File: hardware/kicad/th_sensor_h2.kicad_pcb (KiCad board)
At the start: 2 copper layers, 72 x 58 mm, 74 parts, among them J1 DEBUG, Q1 AO3401A, Q2 AO3401A, Q3 2N7002, Q4 2N7002, SW1 USER/BOOT, SW2 RST, U1 TPS63900DSKR, U2 TPS63900DSKR, U3 TPS3839K33DBZR, U4 ESP32-H2-MINI-1-H4S, U5 SHT40-AD1B-R3, Y1 32.768kHz

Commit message: Finish PCB: silkscreen placement, fab outputs, check reports
- gen_pcb.py: reference designators placed clear of pads, other silk
  and courtyards (rasterised, so concave holder courtyards work); 21
  dense-area references stay on F.Fab only. Cell warning between the
  holders, J1 pinout on the back, tented vias, aux origin at the board
  corner, stitching vias kept clear of pads.
- gen_production.py: Gerber X2 + Excellon (zip), JLC BOM with a dated
  stock/library snapshot, JLC CPL, pad-1 orientation checklist for the
  placement preview, assembly drawing, manufacturing blockers (module
  stock is 0 at JLC on 2026-10-29).
- gen_reports.py: ERC, DRC with schematic parity (0 violations, 0
  unconnected, 0 footprint errors), schematic PDF, 2D/3D renders.

Co-Authored-By: Claude Opus 5.5 <noreply@anthropic.com>
Claude-Session: https://claude.ai/code/session_01TvrXHUQLozvfXGbtsTcbbw
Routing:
- net GND: vias 176 -> 169
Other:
- outline, holes or cut-outs redrawn
- board text added: "2 x CR2032 (one TPS63900 buck-boost per cell)"
- board text added: "3V3"
- board text added: "BOOT"
- board text added: "CR2032 ONLY"
- board text added: "D+"
- board text added: "D-"
- board text added: "ESP32-H2 Matter/Thread temperature & humidity"
- board text added: "GND"
- board text added: "J1 debug (not fitted): 3V3 pad powers the board only with JP1 closed"
- board text added: "NO RECHARGE"
- board text added: "Primary lithium cells only - never recharge"
- board text added: "RX"
- board text added: "TX"
- board text removed: "+"
- board text removed: "2 x CR2032 in parallel through one buck-boost each - do not recharge"
- board text removed: "CR2032 ONLY - NO CHARGE"
- board text removed: "TX RX D+ D- BOOT 3V3 GND"

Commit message: Add EN test pad and net-name test pad labels; reproducible PCB output
Hardware
- TP11 on EN next to the reset button (schematic + PCB); TP9 (GND) moved
  to make room. Schematic: split the EN wire at the new T so kicad-cli
  connects it; fix stale notes (GPIO12 enables the dividers, EN is on
  TP11, not on J1).
- Silkscreen: every test pad shows its net name (VBAT1, VBAT2, VIN1/2,
  VOUT1/2, 3V3_PWR, 3V3, GND, EN); TP numbers stay on the fab drawing.
  "NO CHARGE" under "CR2032 ONLY" as specified, "USER/BOOT" at SW1,
  R1/R11/R21 current links labelled first. Missing required labels now
  stop the generator instead of being dropped.
- gen_pcb.py seeds KiCad's UUID generator, so regenerating gives a
  byte-identical board (KiCad saves items sorted by UUID).
- ERC 0, DRC 0 violations / 0 unconnected / 0 parity errors.

Firmware
- `status` prints free and minimum free heap (bring-up test T-17).

Docs
- README with status table, build/flash/regeneration steps.
- Test plan, architecture, decisions, pin map, assembly, limitations
  updated for TP11, the silkscreen labels, the VBAT_OR equivalence,
  the prod overlay build and disabled secure boot / flash encryption.

Co-Authored-By: Claude Opus 5.5 <noreply@anthropic.com>
Claude-Session: https://claude.ai/code/session_01TvrXHUQLozvfXGbtsTcbbw
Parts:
- added TP11: EN, TestPoint:TestPoint_Pad_D1.5mm, F.Cu at (108.0, 95.8)
- moved TP9 12.3 mm to (121.0, 93.2)
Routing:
- net /EN: track 28.5 -> 35.7 mm
- net /VBAT2: track 63.2 -> 66.6 mm
- net GND: vias 169 -> 168
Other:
- board text added: "NO CHARGE"
- board text added: "USER/BOOT"
- board text removed: "NO RECHARGE"
- board text removed: "USER"

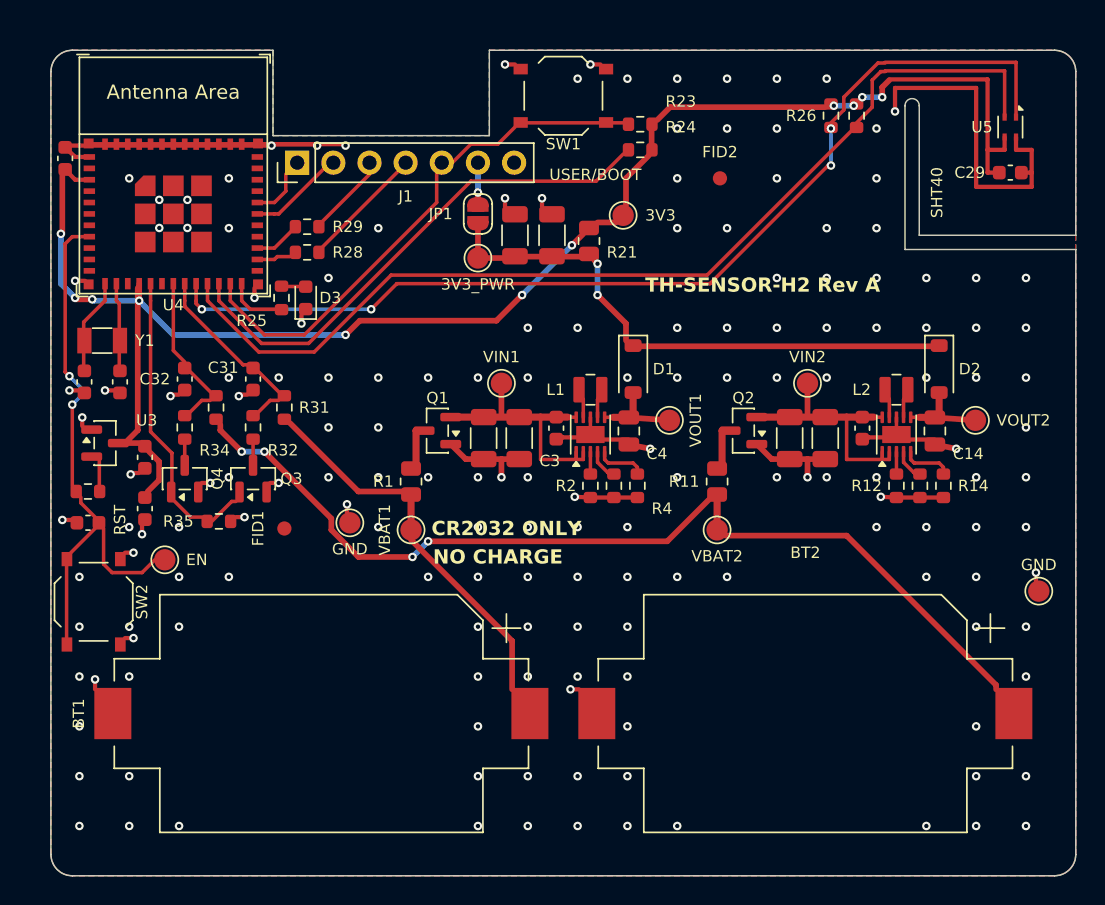
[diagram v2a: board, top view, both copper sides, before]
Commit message: Rev B: one CR2450, 41.5 x 57.5 mm board
Power path: one CR2450 in an SMT holder (MYOUNG BS-24-B4AA016) ->
0R link -> AO3401A reverse-polarity FET -> one TPS63900 at 3.3 V
(SEL = GND, RCFG3 16.2k; 100 mA input limit) -> VOUT -> 0R link ->
+3V3. No output diode: the cell is the only source. Input buffer
10 uF + 2 x 100 uF MLCC + 470 uF electrolytic. J1 shrinks to 1x6 pads
without a supply pin; test pads VBAT, VIN, VOUT, 3V3, GND, EN.

Board: 72 x 58 mm -> 41.5 x 57.5 mm, holder along the bottom edge,
converter block rotated 180 degrees, SHT40 tongue cut free by one
L-shaped slot. 0 unrouted, ERC/DRC/parity 0; the pours are refilled
under the final project rules before the board is saved.
Silkscreen: front "CR2450 ONLY / NO CHARGE" above the holder, label
placer follows arcs instead of their bounding boxes and tries finer
offsets; R1/R21 link labels are now required.

Firmware: one VBAT channel (GPIO5 / ADC1_CH4), BAT_CELL_COUNT 1,
Power Source reports 1 x CR2450 (620 mAh), single-cell logs/status,
host tests and check_pinmap updated.

Power model: architecture S (one cell); CR2450 resistance scaled
from the CR2032 fit by electrode area (ESTIMATE, bounds x0.4/x1.0).
JLC parts snapshot refreshed 2026-10-30 06:47 UTC.

Co-Authored-By: Claude Opus 5.5 <noreply@anthropic.com>
Claude-Session: https://claude.ai/code/session_01TvrXHUQLozvfXGbtsTcbbw
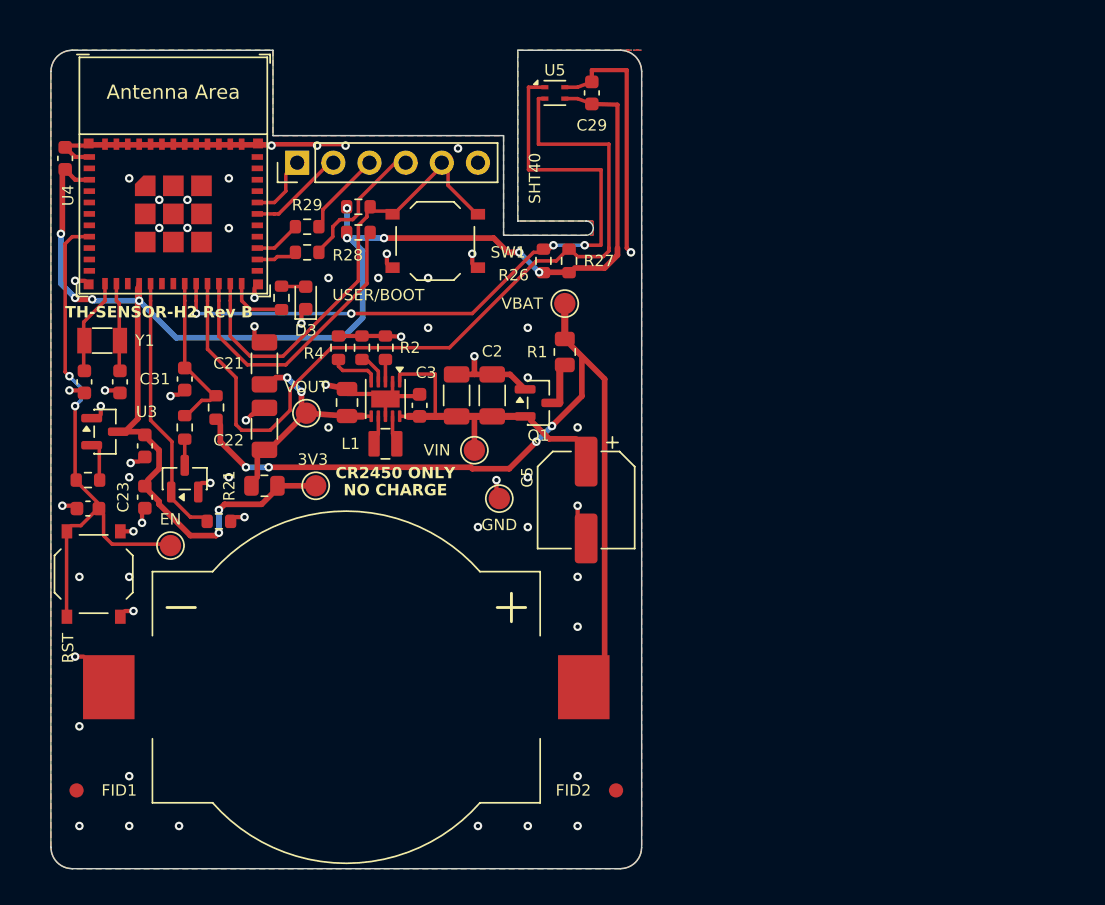
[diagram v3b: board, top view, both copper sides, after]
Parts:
- removed BT2: CR2032 holder, Battery:BatteryHolder_Keystone_1060_1x2032
- removed C11: 10uF, Capacitor_SMD:C_0603_1608Metric
- removed C12, C13: 100uF, Capacitor_SMD:C_1206_3216Metric
- removed C14: 22uF, Capacitor_SMD:C_0805_2012Metric
- removed C32: 22nF, Capacitor_SMD:C_0603_1608Metric
- removed D1, D2: B5819W, Diode_SMD:D_SOD-123
- removed JP1: DEBUG_PWR, Jumper:SolderJumper-2_P1.3mm_Open_RoundedPad1.0x1.5mm
- removed L2: 2.2uH, th_sensor:L_Murata_DFE201612E
- removed Q2: AO3401A, Package_TO_SOT_SMD:SOT-23
- removed Q4: 2N7002, Package_TO_SOT_SMD:SOT-23
- removed R11: 0R, Resistor_SMD:R_0805_2012Metric
- removed R12: 0R, Resistor_SMD:R_0603_1608Metric
- removed R13: 10.5k, Resistor_SMD:R_0603_1608Metric
- removed R14: 16.2k, Resistor_SMD:R_0603_1608Metric
- removed R33, R34: 470k, Resistor_SMD:R_0603_1608Metric
- removed TP10, TP9: GND, TestPoint:TestPoint_Pad_D1.5mm
- removed TP11: EN, TestPoint:TestPoint_Pad_D1.5mm
- removed TP7: 3V3_PWR, TestPoint:TestPoint_Pad_D1.5mm
- removed TP8: 3V3, TestPoint:TestPoint_Pad_D1.5mm
- removed U2: TPS63900DSKR, Package_SON:WSON-10-1EP_2.5x2.5mm_P0.5mm_EP1.2x2mm
- added C5: 470uF, Capacitor_SMD:CP_Elec_6.3x7.7, F.Cu at (137.6, 91.6)
- BT1: value CR2032 holder -> CR2450 holder; footprint Battery:BatteryHolder_Keystone_1060_1x2032 -> th_sensor:BatteryHolder_MYOUNG_BS-24-B4AA016_1x2450
- J1: footprint Connector_PinHeader_2.54mm:PinHeader_1x07_P2.54mm_Vertical -> Connector_PinHeader_2.54mm:PinHeader_1x06_P2.54mm_Vertical
- TP1: value VBAT1 -> VBAT
- TP2: value VBAT2 -> VIN
- TP3: value VIN1 -> VOUT
- TP4: value VIN2 -> 3V3
- TP5: value VOUT1 -> GND
- TP6: value VOUT2 -> EN
- moved TP6 57.2 mm to (108.4, 94.8)
- moved FID2 43.6 mm to (139.7, 112.0)
- moved TP4 35.3 mm to (118.6, 90.6)
- moved U5 32.1 mm to (135.4, 63.0), turned to 0 degrees
- moved C29 29.9 mm to (138.0, 63.0), turned to 90 degrees
- moved R21 28.6 mm to (115.0, 90.6), turned to 0 degrees
- moved C22 24.4 mm to (115.0, 86.6)
- moved FID1 23.5 mm to (101.8, 112.0)
- moved R4 23.1 mm to (120.2, 80.9), turned to 90 degrees
- moved R26 22.6 mm to (134.6, 74.8), turned to 90 degrees
- moved R27 22.6 mm to (136.4, 74.8), turned to 90 degrees
- moved R23 20.6 mm to (121.6, 71.0), turned to 0 degrees
- moved R24 20.6 mm to (121.6, 72.8), turned to 0 degrees
- moved R3 20.2 mm to (121.8, 80.9), turned to 90 degrees
- moved C4 19.9 mm to (120.8, 84.8), turned to 90 degrees
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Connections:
- net /CFG1_1 renamed /CFG1
- net /CFG2_1 renamed /CFG2
- net /CFG3_1 renamed /CFG3
- net /LX1_1 renamed /LX1
- net /LX2_1 renamed /LX2
- net /SNS1_LO renamed /SNS_LO
- net /VBAT1 renamed /VBAT
- net /VBAT1_L renamed /VBAT_L
- net /VBAT1_SENSE renamed /VBAT_SENSE
- C1 pad 1: /VIN1 -> /VIN
- C2 pad 1: /VIN1 -> /VIN
- C21 pad 1: /3V3_PWR -> /VOUT
- C22 pad 1: /3V3_PWR -> /VOUT
- C3 pad 1: /VIN1 -> /VIN
- C4 pad 1: /VOUT1 -> /VOUT
- J1 pad 6: /3V3_DBG -> GND
- Q1 pad 2: /VIN1 -> /VIN
- R21 pad 1: /3V3_PWR -> /VOUT
- TP2 pad 1: /VBAT2 -> /VIN
- TP3 pad 1: /VIN1 -> /VOUT
- TP4 pad 1: /VIN2 -> +3V3
- TP5 pad 1: /VOUT1 -> GND
- TP6 pad 1: /VOUT2 -> /EN
- U1 pad 1: /VIN1 -> /VIN
- U1 pad 10: /VIN1 -> /VIN
- U1 pad 2: /VIN1 -> GND
- U1 pad 6: /VOUT1 -> /VOUT
- U4 pad 18: /VBAT2_SENSE -> unconnected-(U4-GPIO4/FSPICLK/ADC1_CH3/MTCK-Pad18)
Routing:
- net /VBAT2: track 66.6 -> 0.00 mm, vias 4 -> 0
- net /VBAT: track 25.8 -> 57.6 mm, vias 0 -> 4
- net /3V3_PWR: track 31.6 -> 0.00 mm, vias 2 -> 0
- net GND: track 111.0 -> 87.7 mm, vias 168 -> 62
- net /I2C_SDA: track 72.1 -> 49.0 mm
- net /VIN: track 0.00 -> 20.9 mm
- net /VIN2: track 18.2 -> 0.00 mm
- net /VIN1: track 18.2 -> 0.00 mm
- net /STRAP_GPIO8: track 36.4 -> 20.5 mm
- net /I2C_SCL: track 70.6 -> 58.7 mm
- net /VOUT: track 0.00 -> 11.5 mm, vias 0 -> 2
- net /VBAT2_SENSE: track 9.54 -> 0.00 mm
- net /VOUT2: track 6.61 -> 0.00 mm
- net /VOUT1: track 6.61 -> 0.00 mm
- net /BTN_USER: track 34.1 -> 28.4 mm
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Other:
- board size 72 x 58 mm -> 41.5 x 57.5 mm
- board text added: "1 x CR2450, TPS63900 3.3 V"
- board text added: "CR2450 ONLY"
- board text added: "CR2450 ONLY - NO CHARGE"
- board text added: "ESP32-H2 Matter/Thread"
- board text added: "J1 debug (not fitted): no supply pin,"
- board text added: "TH-SENSOR-H2 Rev B"
- board text added: "TH-SENSOR-H2 Rev B 2026-10-30"
- board text added: "primary lithium cell - never recharge"
- board text added: "temperature & humidity"
- board text added: "the cell powers the board"
- board text removed: "2 x CR2032 (one TPS63900 buck-boost per cell)"
- board text removed: "3V3"
- board text removed: "CR2032 ONLY"
- board text removed: "ESP32-H2 Matter/Thread temperature & humidity"
- board text removed: "J1 debug (not fitted): 3V3 pad powers the board only with JP1 closed"
- board text removed: "Primary lithium cells only - never recharge"
- board text removed: "TH-SENSOR-H2 Rev A"
- board text removed: "TH-SENSOR-H2 Rev A 2026-10-29"
